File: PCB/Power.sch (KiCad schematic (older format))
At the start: 0 parts

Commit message: Progress
Datasheets added for regulators, regulators chosen, more datasheets
ralted to Zync 7000 added. Memory module chose footprint created and
datasheet added. Schematic work in progress. Project is slow going do to
th sheer amount of documenation to absorb on the Zync and makign high
pin count BGAs is tedious. More to follow soon.
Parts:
- added C?: CL10A106KQ8NNNC, PCB_Footprints:C0603, symbol CL10A106KQ8NNNC
- added C?: CL31B106KLHNNNE, PCB_Footprints:C1206, symbol CL31B106KLHNNNE
- added L? (x3): XFL3012-222MEC, PCB_Footprints:XFL3012-222MEC, symbol XFL3012-222MEC
- added R?: ERJ-2RKF1003X, PCB_Footprints:R0402, symbol ERJ-2RKF1003X
- added U?: TPS62142RGTR, PCB_Footprints:TPS62142RGTR, symbol TPS62142RGTR
- added U?: TPS622313DRYT, PCB_Footprints:TPS622313DRYT, symbol TPS622313DRYT
- added U?: TPS62293DRVR, PCB_Footprints:TPS62293DRVR, symbol TPS62293DRVR
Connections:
- net labels added: +12V, GND
- wire segments 0 -> 13

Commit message: Power Supply
Power supply components researched and selected. Power supply schematic
completed except for input section, currently all voltage regulators
implemented.
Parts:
- removed C?: CL10A106KQ8NNNC, PCB_Footprints:C0603, symbol CL10A106KQ8NNNC
- removed C?: CL31B106KLHNNNE, PCB_Footprints:C1206, symbol CL31B106KLHNNNE
- removed L? (x3): XFL3012-222MEC, PCB_Footprints:XFL3012-222MEC, symbol XFL3012-222MEC
- added C?: CL05A475KQ5NRNC, PCB_Footprints:C0402, symbol CL05A475KQ5NRNC
- added C?: CL32B106KBJNNWE, PCB_Footprints:C1210, symbol CL32B106KBJNNWE
- added C?: CL10C332JA8NNNC, PCB_Footprints:C0603, symbol CL10C332JA8NNNC
- added C?: CL21A226KQQNNNE, PCB_Footprints:C0805, symbol CL21A226KQQNNNE
- added C?: C0603C220D5GACTU, PCB_Footprints:C0603, symbol C0603C220D5GACTU
- added C?: CL05B104JP5NNNC, PCB_Footprints:C0402, symbol CL05B104JP5NNNC
- added C?: CL10A225KQ8NNNC, PCB_Footprints:C0603, symbol CL10A225KQ8NNNC
- added L?: XFL4020-222ME_, PCB_Footprints:XFL4020-222ME_, symbol XFL4020-222ME_
- added L?: LPS3015-222MR_, PCB_Footprints:LPS3015-222MR_, symbol LPS3015-222MR_
- added L?: LQM2HPN1R0MJ0L, PCB_Footprints:LQM2HPN1R0MJ0L, symbol LQM2HPN1R0MJ0L
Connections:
- net labels added: +1V35, +1V8, +3.3V
- wire segments 13 -> 32
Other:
- note added: "1A 1.8V DCDC Regulator 6V Input MAX"
- note added: "2A 3.3V DCDC Regulator 17V Input MAX"
- note added: "500mA 1.8V DCDC Regulator 6V Input MAX"
- note added: "Supposed to be 1.3V but KiCAD is fucky about that \n"
- note added: "System Power Supply"

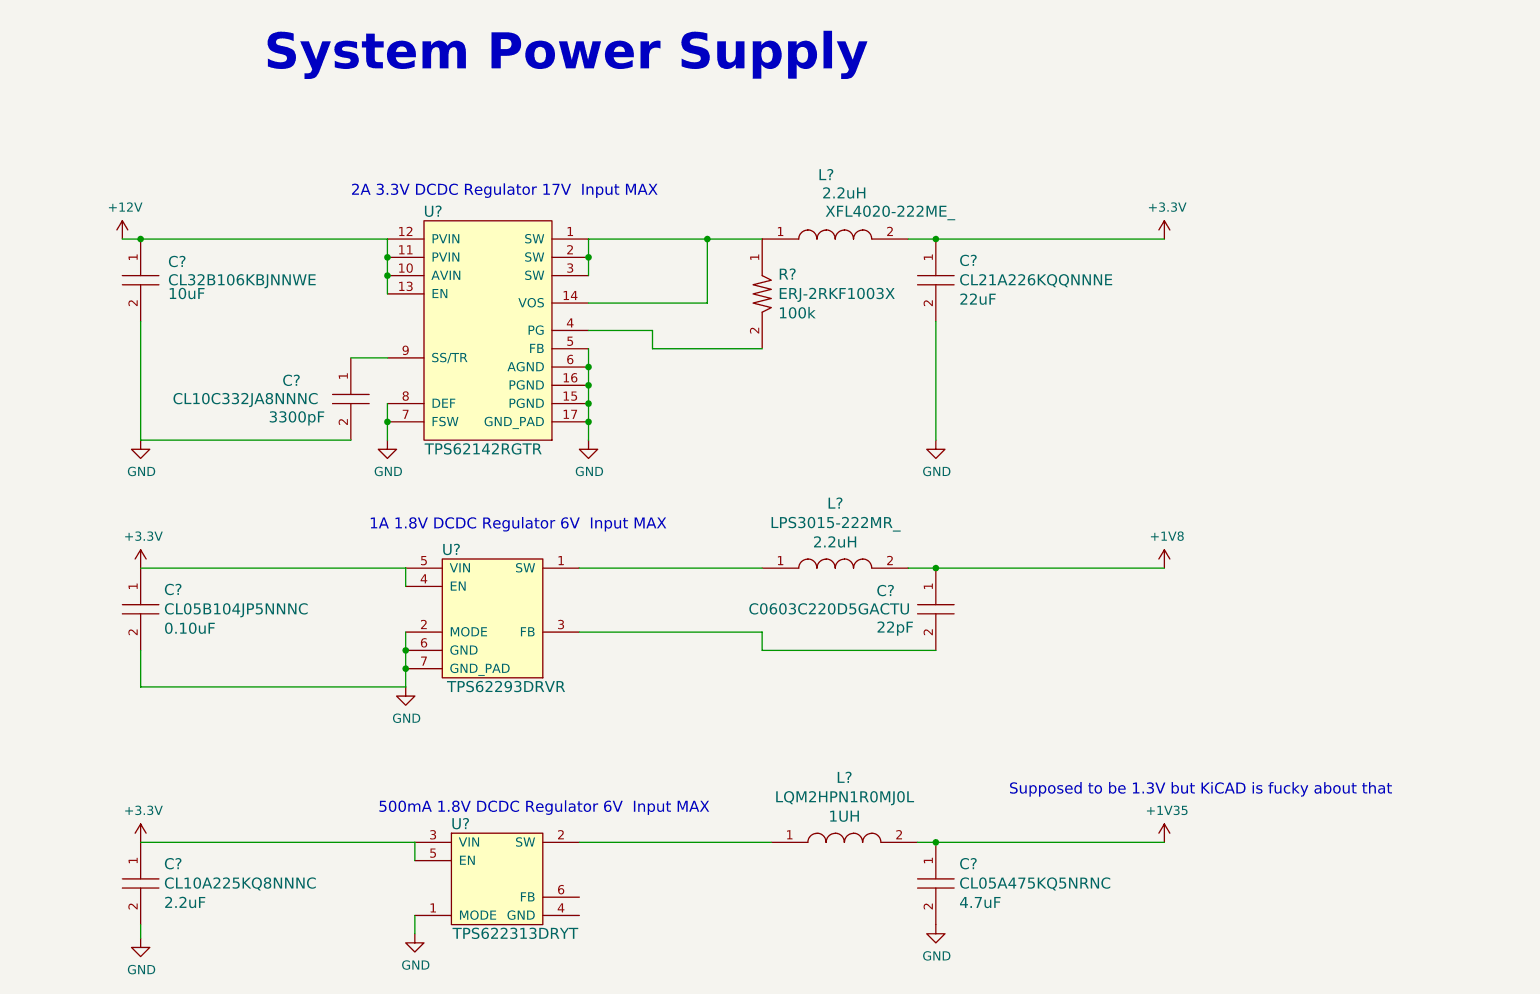
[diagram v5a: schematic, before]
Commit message: PMIC progress
More progress made on the implemenation of the PMIC schematic from the
Ti reference notes. Currently researching a 5V DCDC and input power
circuit that can switch between USB bus power and external power.
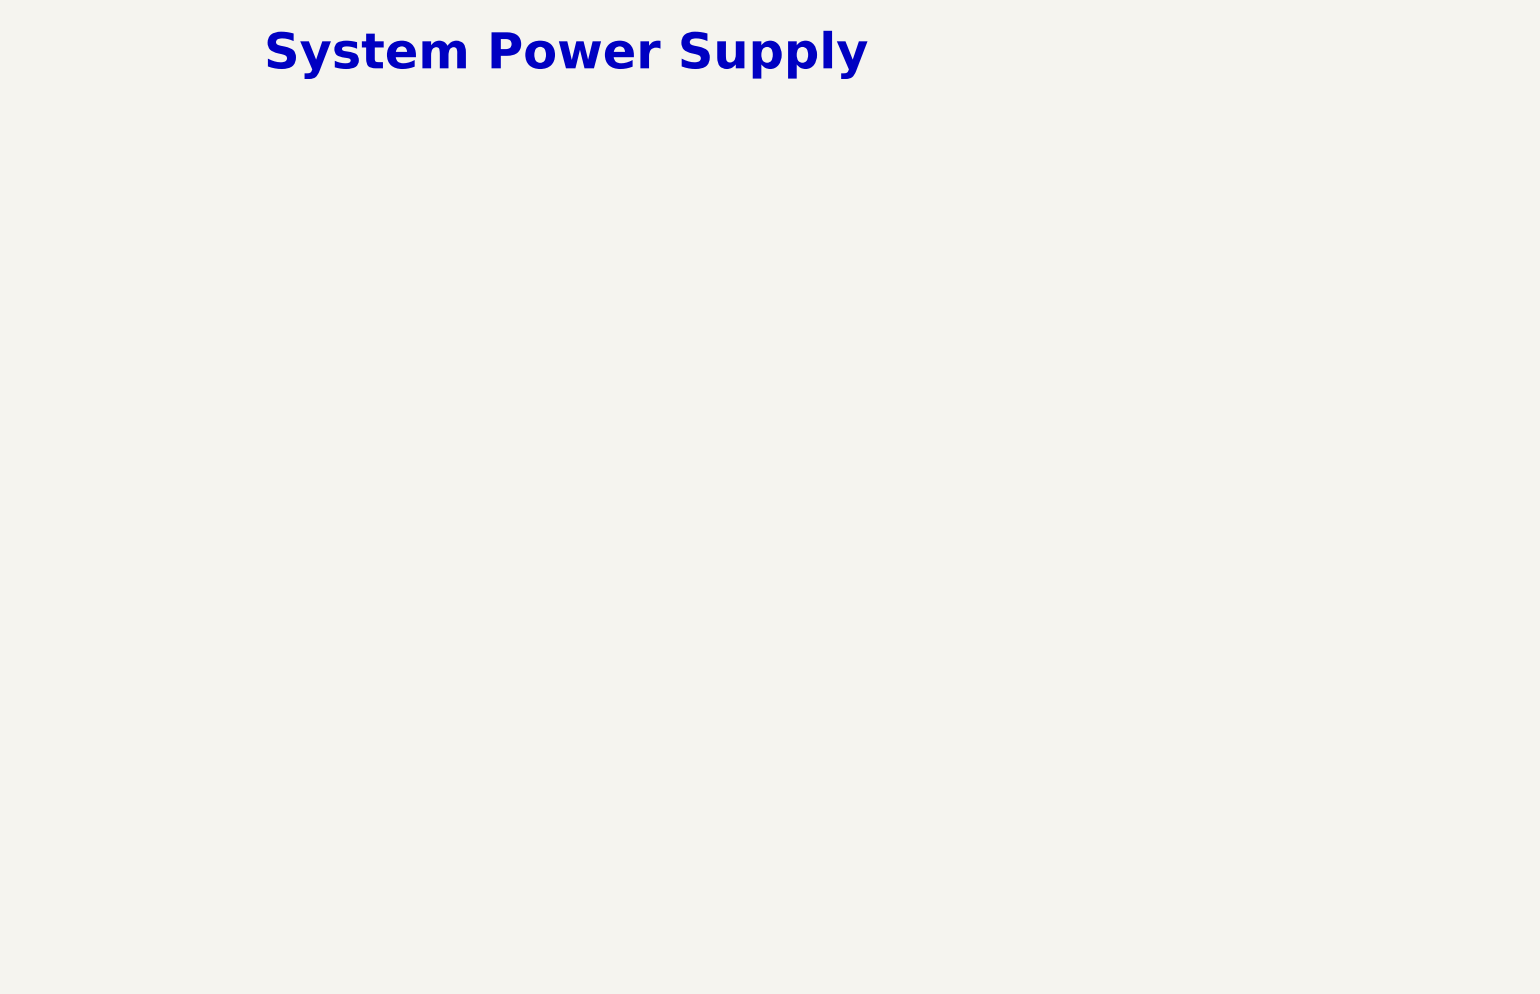
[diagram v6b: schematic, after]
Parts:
- removed C?: CL05A475KQ5NRNC, PCB_Footprints:C0402, symbol CL05A475KQ5NRNC
- removed C?: CL32B106KBJNNWE, PCB_Footprints:C1210, symbol CL32B106KBJNNWE
- removed C?: CL10C332JA8NNNC, PCB_Footprints:C0603, symbol CL10C332JA8NNNC
- removed C?: CL21A226KQQNNNE, PCB_Footprints:C0805, symbol CL21A226KQQNNNE
- removed C?: C0603C220D5GACTU, PCB_Footprints:C0603, symbol C0603C220D5GACTU
- removed C?: CL05B104JP5NNNC, PCB_Footprints:C0402, symbol CL05B104JP5NNNC
- removed C?: CL10A225KQ8NNNC, PCB_Footprints:C0603, symbol CL10A225KQ8NNNC
- removed L?: XFL4020-222ME_, PCB_Footprints:XFL4020-222ME_, symbol XFL4020-222ME_
- removed L?: LPS3015-222MR_, PCB_Footprints:LPS3015-222MR_, symbol LPS3015-222MR_
- removed L?: LQM2HPN1R0MJ0L, PCB_Footprints:LQM2HPN1R0MJ0L, symbol LQM2HPN1R0MJ0L
- removed R?: ERJ-2RKF1003X, PCB_Footprints:R0402, symbol ERJ-2RKF1003X
- removed U?: TPS62142RGTR, PCB_Footprints:TPS62142RGTR, symbol TPS62142RGTR
- removed U?: TPS622313DRYT, PCB_Footprints:TPS622313DRYT, symbol TPS622313DRYT
- removed U?: TPS62293DRVR, PCB_Footprints:TPS62293DRVR, symbol TPS62293DRVR
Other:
- note removed: "1A 1.8V DCDC Regulator 6V Input MAX"
- note removed: "2A 3.3V DCDC Regulator 17V Input MAX"
- note removed: "500mA 1.8V DCDC Regulator 6V Input MAX"
- note removed: "Supposed to be 1.3V but KiCAD is fucky about that \n"
